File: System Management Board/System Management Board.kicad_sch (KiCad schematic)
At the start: 25 parts, among them J1 Conn_01x04_Male, J2 Conn_01x02_Male, J3 Conn_01x04_Male, J4 Barrel_Jack, J5 Conn_02x06_Counter_Clockwise, J6 Conn_02x20_Odd_Even, K1 J115F11CH5VDCS61.5U, K2 J114FL1CS165VDC.41, K3 J114FL1CS165VDC.41, U1 SC0915, U2 OKI-78SR-5{slash}1.5-W36E-C, U3 OKI-78SR-5{slash}1.5-W36E-C

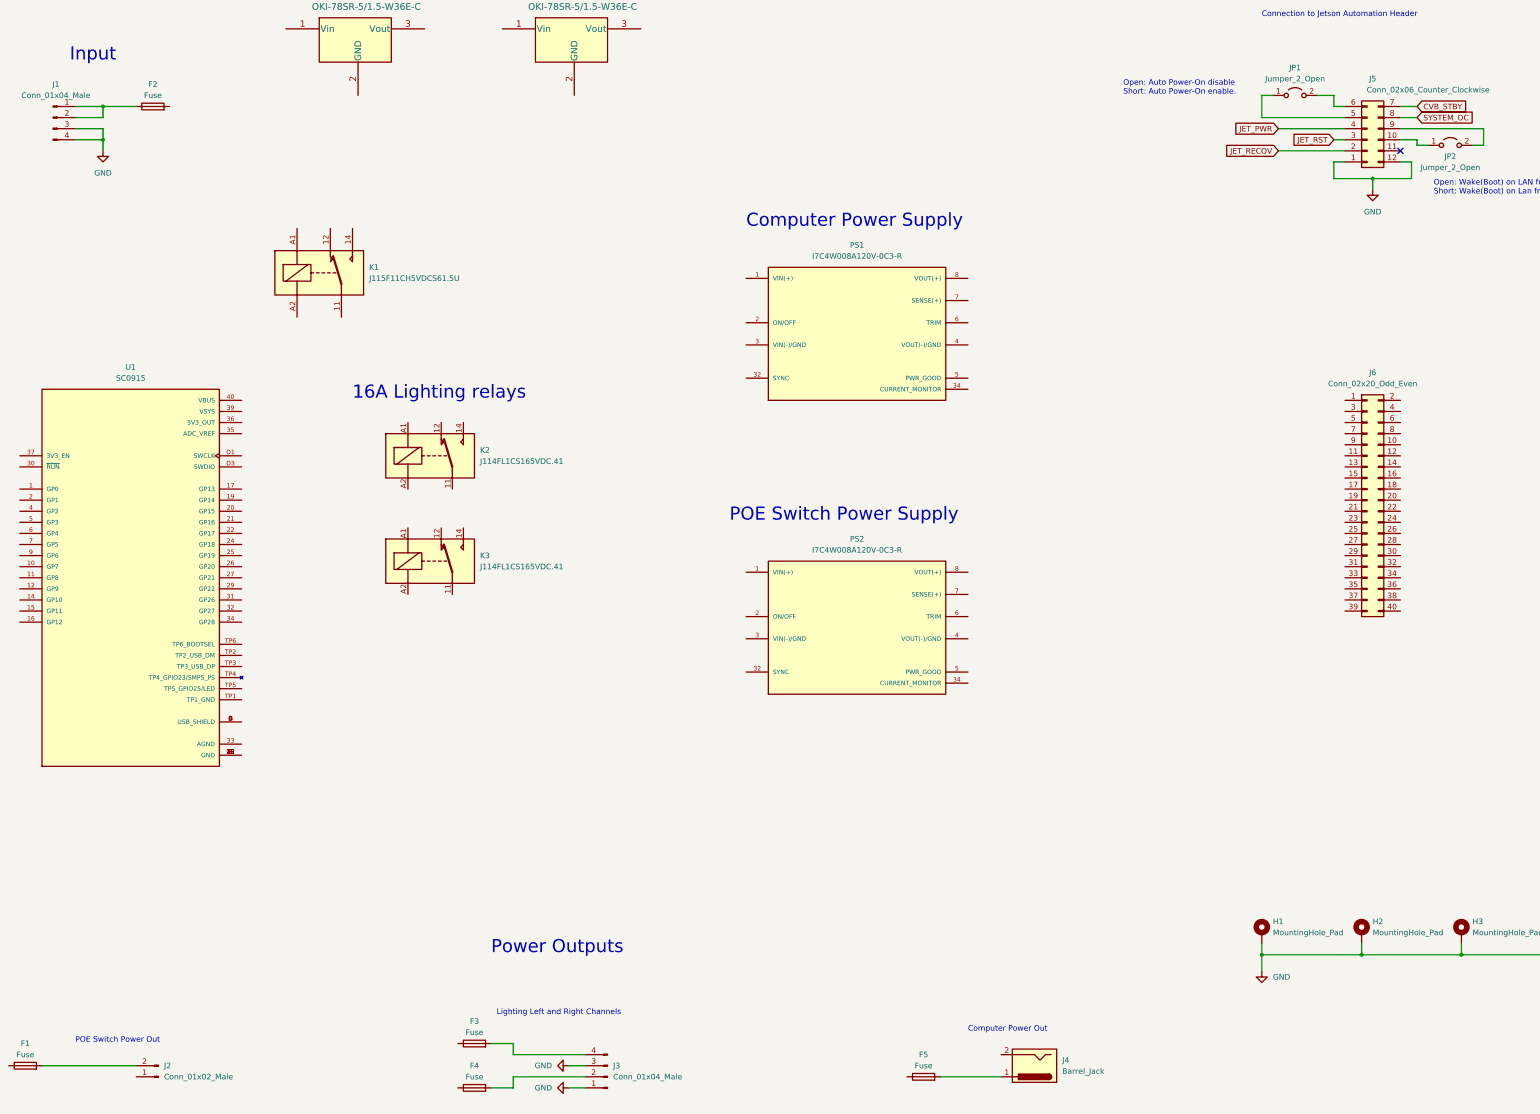
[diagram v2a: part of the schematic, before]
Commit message: Worked on importing KiCad parts and major componet layout
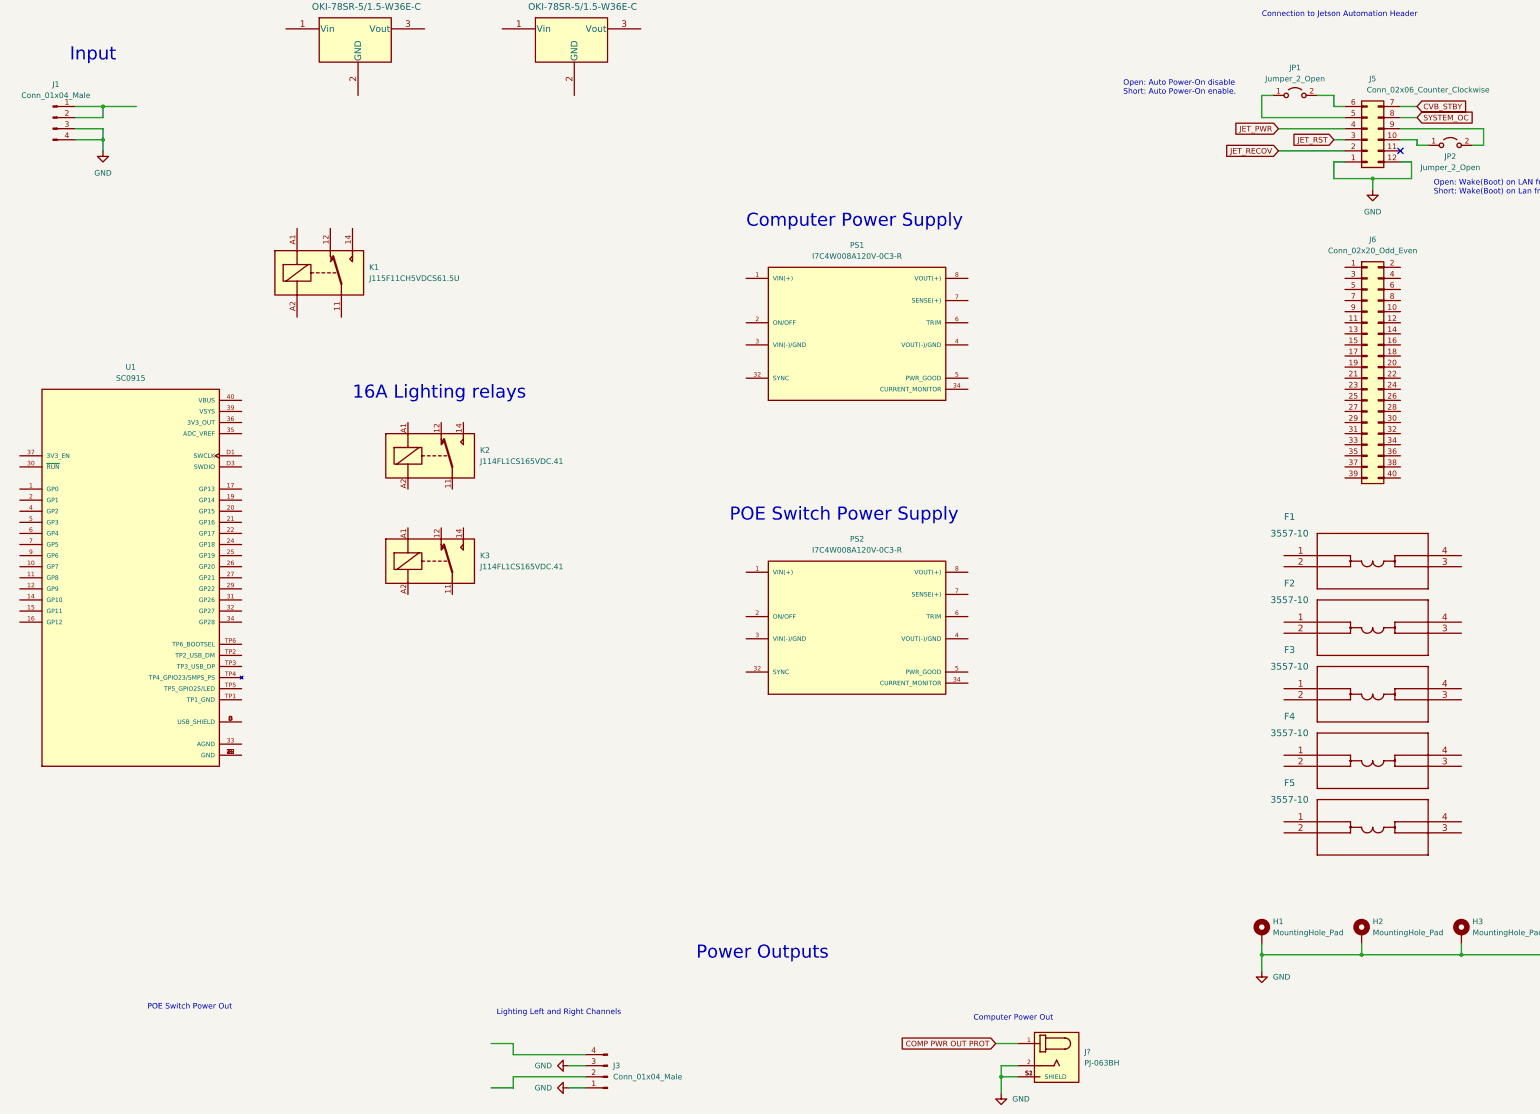
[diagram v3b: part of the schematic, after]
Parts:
- removed F1, F2, F3, F4, F5: Fuse, symbol Device:Fuse
- removed J2: Conn_01x02_Male, symbol Connector:Conn_01x02_Male
- removed J4: Barrel_Jack, symbol Connector:Barrel_Jack
- added F1, F2, F3, F4, F5: 3557-10, SMB:3557-10, symbol SMB:3557-10
- added J?: PJ-063BH, CUI_PJ-063BH, symbol SMB:PJ-063BH
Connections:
- net GND: now also J?.2, J?.S1 (SHIELD), J?.S2 (SHIELD)
- new net COMP PWR OUT PROT: J?.1
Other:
- moved on the sheet: J6

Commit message: Added more parts to SMB KiCad, worked on schematic and power supplies
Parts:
- added C? (x6): 100uF, symbol Device:C_Polarized
- added C? (x4): 10uF, Capacitor_SMD:C_1210_3225Metric, symbol Device:C
- added C? (x4): 270uF, symbol Device:C_Polarized
- added C? (x4): 0.1uF, Capacitor_SMD:C_1210_3225Metric, symbol Device:C
- added J3, J5: Conn_01x02_Male, SMB:1843606, symbol Connector:Conn_01x02_Male
- added R? (x2): 1k, symbol Device:R
- added R?: 4.64k, symbol Device:R
- added R?: 28, symbol Device:R
- added U4: NEO-M9N-00B, SMB:XCVR_NEO-M9N-00B, symbol SMB:NEO-M9N-00B
- J1: footprint (none) -> SMB:1924321
- J2: renamed from J3; footprint (none) -> SMB:1924321
- J4: renamed from J?; footprint CUI_PJ-063BH -> SMB:CUI_PJ-063BH
- J6: renamed from J5; footprint (none) -> Connector_PinHeader_2.54mm:PinHeader_2x06_P2.54mm_Vertical
- JP1, JP2: footprint (none) -> Connector_PinHeader_2.54mm:PinHeader_1x02_P2.54mm_Vertical
- renumbered J6 to J7
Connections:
- net COMP PWR OUT PROT: now also F4.3, F4.4, J5.1 (Pin_1)
- net GND: now also PS1.3 (VIN(-)/GND), PS1.32 (SYNC), PS1.4 (VOUT(-)/GND), PS2.3 (VIN(-)/GND), PS2.32 (SYNC), PS2.4 (VOUT(-)/GND), C?.2, C?.2, C?.2, C?.2, C?.2, C?.2, C?.2, C?.2, C?.2, C?.2, C?.2, C?.2, C?.2, C?.2, C?.2, C?.2, C?.2, C?.2, J3.1 (Pin_1), J5.2 (Pin_2), R?.1, R?.1, R?.2, R?.2
- net LIGHT BANK B PROT SW: now reaches J2.2 (Pin_2)
- net LIGHT BANK B PROT SW: now also K3.14
- net LIGHT BANK A PROT SW: now reaches J2.4 (Pin_4)
- net LIGHT BANK A PROT SW: now also K2.14
- net V_batt+: now reaches F1.1
- net V_batt+: now also F1.2, J1.1 (Pin_1), J1.2 (Pin_2)
- net V_batt+ PROT: now reaches F1.3
- net V_batt+ PROT: now also F1.4, K1.11
- net LIGHT BANK A PROT: now reaches K2.11
- net LIGHT BANK A PROT: now also F2.3, F2.4
- net LIGHT BANK B PROT: now reaches K3.11
- net LIGHT BANK B PROT: now also F3.3, F3.4
- net V_batt+ PROT SW: now reaches F2.1
- net V_batt+ PROT SW: now also F2.2, F3.1, F3.2, K1.14, PS1.1 (VIN(+)), PS2.1 (VIN(+)), C?.1, C?.1, C?.1, C?.1, C?.1, C?.1, C?.1, C?.1
- net SWITCH PWR OUT: now reaches F5.1
- net SWITCH PWR OUT: now also F5.2, PS2.7 (SENSE(+)), PS2.8 (VOUT(+)), C?.1, C?.1, C?.1, C?.1
- net SWITCH PWR OUT PROT: now reaches F5.3
- net SWITCH PWR OUT PROT: now also F5.4, J3.2 (Pin_2)
- net COMP PWR OUT: now reaches F4.1
- net COMP PWR OUT: now also F4.2, PS1.7 (SENSE(+)), PS1.8 (VOUT(+)), C?.1, C?.1, C?.1, C?.1
- net ~{SWITCH PWR EN}: now reaches PS2.2 (ON/OFF)
- net at PS2.34 (CURRENT_MONITOR): now also C?.1, R?.2
- net SWITCH PWR GOOD: now reaches PS2.5 (PWR_GOOD)
- net at PS2.6 (TRIM): now also R?.1
- net ~{COMP PWR EN}: now reaches PS1.2 (ON/OFF)
- net at PS1.34 (CURRENT_MONITOR): now also C?.1, R?.2
- net COMP PWR GOOD: now reaches PS1.5 (PWR_GOOD)
- net at PS1.6 (TRIM): now also R?.1
- new net: U4.10 (GND), U4.12 (GND), U4.13 (GND), U4.24 (GND)
- new net: U4.15 (RESERVED), U4.16 (RESERVED), U4.17 (RESERVED)
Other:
- note added: "15A"
- note added: "40A"
- note added: "50A Main Power Relay"
- note added: "5A"
- note added: "7.5A"
- note added: "Blade Fuses"
- note added: "Computer Power"
- note added: "Lighting Bank A & B"
- note added: "Main Power Input"
- note added: "POE Switch Power"
- note removed: "Computer Power Out"
- note removed: "Input"
- note removed: "Lighting Left and Right Channels"
- note removed: "POE Switch Power Out"
- moved on the sheet: F1, F2, F3, F4, F5, H1, H2, H3, H4, J1, J2, J4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

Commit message: Finished heatspreader and sent to Xometry, solidified postion of DC-DC converters and mounting holes on SMB PCB
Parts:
- added F6, F7: Fuse, SMB:FUSC9830X318N, symbol Device:Fuse
- C1, C10, C11, C12, C15, C16, C2, C3, C4, C9: renamed from C?; footprint (none) -> Capacitor_SMD:CP_Elec_10x12.6
- C13, C14: renamed from C?; footprint Capacitor_SMD:C_1210_3225Metric -> Capacitor_SMD:C_1206_3216Metric
- R1, R2, R3, R4: renamed from R?; footprint (none) -> Resistor_SMD:R_1206_3216Metric
- gave numbers to parts that had none: 6
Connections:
- net GND: now also J1.1 (Pin_1), J1.2 (Pin_2), J2.2 (Pin_2), J2.4 (Pin_4); no longer J1.3 (Pin_3), J1.4 (Pin_4), J2.1 (Pin_1), J2.3 (Pin_3)
- net LIGHT BANK A PROT SW: now also J2.1 (Pin_1); no longer J2.4 (Pin_4)
- net LIGHT BANK B PROT SW: now also J2.3 (Pin_3); no longer J2.2 (Pin_2)
- net V_batt+: now also J1.3 (Pin_3), J1.4 (Pin_4); no longer J1.1 (Pin_1), J1.2 (Pin_2)
- net V_batt+ PROT SW: now also F6.1, F7.1; no longer C1.1, C2.1, C3.1, C4.1, C5.1, C6.1, C7.1, C8.1, PS1.1 (VIN(+)), PS2.1 (VIN(+))
- new net CPS_IN_PROT: C1.1, C3.1, C5.1, C7.1, F6.2, PS1.1 (VIN(+))
- new net PSPS_IN_PROT: C2.1, C4.1, C6.1, C8.1, F7.2, PS2.1 (VIN(+))
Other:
- moved on the sheet: J2

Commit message: Added aux outputs and worked on routing for high current traces
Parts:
- added F8, F9: 3557-10, SMB:3557-10, symbol SMB:3557-10
- added J8, J9: Conn_01x02_Male, SMB:1843606, symbol Connector:Conn_01x02_Male
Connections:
- net COMP PWR OUT PROT: now also J5.2 (Pin_2); no longer J5.1 (Pin_1)
- net GND: now also J5.1 (Pin_1), J8.1 (Pin_1), J9.1 (Pin_1); no longer J5.2 (Pin_2)
- net COMP PWR OUT renamed 15v PWR
- net 15v PWR: now also F8.1, F8.2
- net SWITCH PWR OUT renamed 48V PWR
- net 48V PWR: now also F9.1, F9.2
- new net 15V Aux PWR OUT PROT: F8.3, F8.4, J9.2 (Pin_2)
- new net 48V Aux PWR OUT PROT: F9.3, F9.4, J8.2 (Pin_2)
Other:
- note added: "15V Aux PWR Out"
- note added: "48V Aux PWR Out"
- note added: "TBD"
- moved on the sheet: F1, F2, F3, F4, F5, J1, J2, J3, J4, J5, J7, K1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

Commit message: general SMB schmeatic work
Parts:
- added U?: AP7375-50W5-7, Package_TO_SOT_SMD:SOT-23-5, symbol SMB:AP7375-50W5-7
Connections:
- net GND: now also U2.2 (GND), U3.2 (GND), U?.2 (GND)
- net V_batt+ PROT SW: now also U2.1 (Vin), U3.1 (Vin), U?.1 (Vin)
- net 5V Logic PWR: now reaches U3.3 (Vout)
- net 5V Relay PWR: now reaches U2.3 (Vout)
- net Vin_MES_ADC: now reaches U1.31 (GP26)
- new net Switched PWR IN PROT: U?.3 (EN)
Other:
- moved on the sheet: C1, C10, C11, C12, C13, C14, C15, C16, C17, C18, C2, C3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

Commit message: Removed GPS module, added GPIO connections to headder, added aux jetson header
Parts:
- removed U4: NEO-M9N-00B, SMB:XCVR_NEO-M9N-00B, symbol SMB:NEO-M9N-00B
- added J10: Conn_01x02_Male, SMB:1843606, symbol Connector:Conn_01x02_Male
- added J11: Conn_02x20_Odd_Even, Connector_PinHeader_2.54mm:PinHeader_2x20_P2.54mm_Vertical, symbol Connector_Generic:Conn_02x20_Odd_Even
- gave numbers to parts that had none: 1
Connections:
- net 5V Logic PWR: now also U1.39 (VSYS), U4.5 (Vout)
- net GND: now also J7.14 (Pin_14), J7.20 (Pin_20), J7.25 (Pin_25), J7.30 (Pin_30), J7.34 (Pin_34), J7.39 (Pin_39), J7.6 (Pin_6), J7.9 (Pin_9), J10.1 (Pin_1), J11.14 (Pin_14), J11.20 (Pin_20), J11.25 (Pin_25), J11.30 (Pin_30), J11.34 (Pin_34), J11.39 (Pin_39), J11.6 (Pin_6), J11.9 (Pin_9)
- net Switched PWR IN PROT: now also J10.2 (Pin_2)
- net V_batt+ PROT: now also U4.1 (Vin)
- net V_batt+ PROT SW: no longer U4.1 (Vin)
- net JET_P1: now reaches J7.1 (Pin_1)
- net JET_P1: now also J11.1 (Pin_1)
- net Jet_UART1_Rx: now reaches J7.10 (Pin_10)
- net Jet_UART1_Rx: now also J11.10 (Pin_10)
- net JET_P11: now reaches J7.11 (Pin_11)
- net JET_P11: now also J11.11 (Pin_11)
- net JET_P12: now reaches J7.12 (Pin_12)
- net JET_P12: now also J11.12 (Pin_12)
- net PICO OUT BIT 1: now reaches J7.13 (Pin_13)
- net PICO OUT BIT 1: now also U1.6 (GP4), J11.13 (Pin_13)
- net PICO OUT BIT 0: now reaches J7.15 (Pin_15)
- net PICO OUT BIT 0: now also U1.5 (GP3), J11.15 (Pin_15)
- net PICO IN BIT 0: now reaches J7.16 (Pin_16)
- net PICO IN BIT 0: now also U1.1 (GP0), J11.16 (Pin_16)
- net JET_P17: now reaches J7.17 (Pin_17)
- net JET_P17: now also J11.17 (Pin_17)
- net PICO OUT BIT 2: now reaches J7.18 (Pin_18)
- net PICO OUT BIT 2: now also U1.7 (GP5), J11.18 (Pin_18)
- net JET_P19: now reaches J7.19 (Pin_19)
- net JET_P19: now also J11.19 (Pin_19)
- net JET_P2: now reaches J7.2 (Pin_2)
- net JET_P2: now also J11.2 (Pin_2)
- net JET_P21: now reaches J7.21 (Pin_21)
- net JET_P21: now also J11.21 (Pin_21)
- net PICO IN BIT 2: now reaches J7.22 (Pin_22)
- net PICO IN BIT 2: now also U1.4 (GP2), J11.22 (Pin_22)
- net JET_P23: now reaches J7.23 (Pin_23)
- net JET_P23: now also J11.23 (Pin_23)
- net JET_P24: now reaches J7.24 (Pin_24)
- net JET_P24: now also J11.24 (Pin_24)
- net JET_P26: now reaches J7.26 (Pin_26)
- net JET_P26: now also J11.26 (Pin_26)
- net JET_P27: now reaches J7.27 (Pin_27)
- net JET_P27: now also J11.27 (Pin_27)
- net JET_P28: now reaches J7.28 (Pin_28)
- net JET_P28: now also J11.28 (Pin_28)
- net JET_P29: now reaches J7.29 (Pin_29)
- net JET_P29: now also J11.29 (Pin_29)
- net JET_P3: now reaches J7.3 (Pin_3)
- net JET_P3: now also J11.3 (Pin_3)
- net JET_P31: now reaches J7.31 (Pin_31)
- net JET_P31: now also J11.31 (Pin_31)
- net PICO IN BIT 1: now reaches J7.32 (Pin_32)
- net PICO IN BIT 1: now also U1.2 (GP1), J11.32 (Pin_32)
- net JET_P33: now reaches J7.33 (Pin_33)
- net JET_P33: now also J11.33 (Pin_33)
- net JET_P35: now reaches J7.35 (Pin_35)
- net JET_P35: now also J11.35 (Pin_35)
- net JET_P36: now reaches J7.36 (Pin_36)
- net JET_P36: now also J11.36 (Pin_36)
- net JET_P37: now reaches J7.37 (Pin_37)
- net JET_P37: now also J11.37 (Pin_37)
- net JET_P38: now reaches J7.38 (Pin_38)
- net JET_P38: now also J11.38 (Pin_38)
- net JET_P4: now reaches J7.4 (Pin_4)
- net JET_P4: now also J11.4 (Pin_4)
- net JET_P40: now reaches J7.40 (Pin_40)
- net JET_P40: now also J11.40 (Pin_40)
- net JET_P5: now reaches J7.5 (Pin_5)
- net JET_P5: now also J11.5 (Pin_5)
- net JET_P7: now reaches J7.7 (Pin_7)
- net JET_P7: now also J11.7 (Pin_7)
- net Jet_UART1_Tx: now reaches J7.8 (Pin_8)
- net Jet_UART1_Tx: now also J11.8 (Pin_8)
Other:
- note added: "Auxiallary Jetson Header"
- note added: "Jetson Header"
- note added: "Switched power on wakeup"
- moved on the sheet: J7, U1, U2, U3, U4
